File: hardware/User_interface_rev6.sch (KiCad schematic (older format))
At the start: 42 parts, among them IC201 CAT4002ATD-GT3, SW201 F1, SW202 F4, SW203 F7, SW204 ESTOP, SW205 F0, SW206 F2, SW207 F5, SW208 F8, SW209 LOCO1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

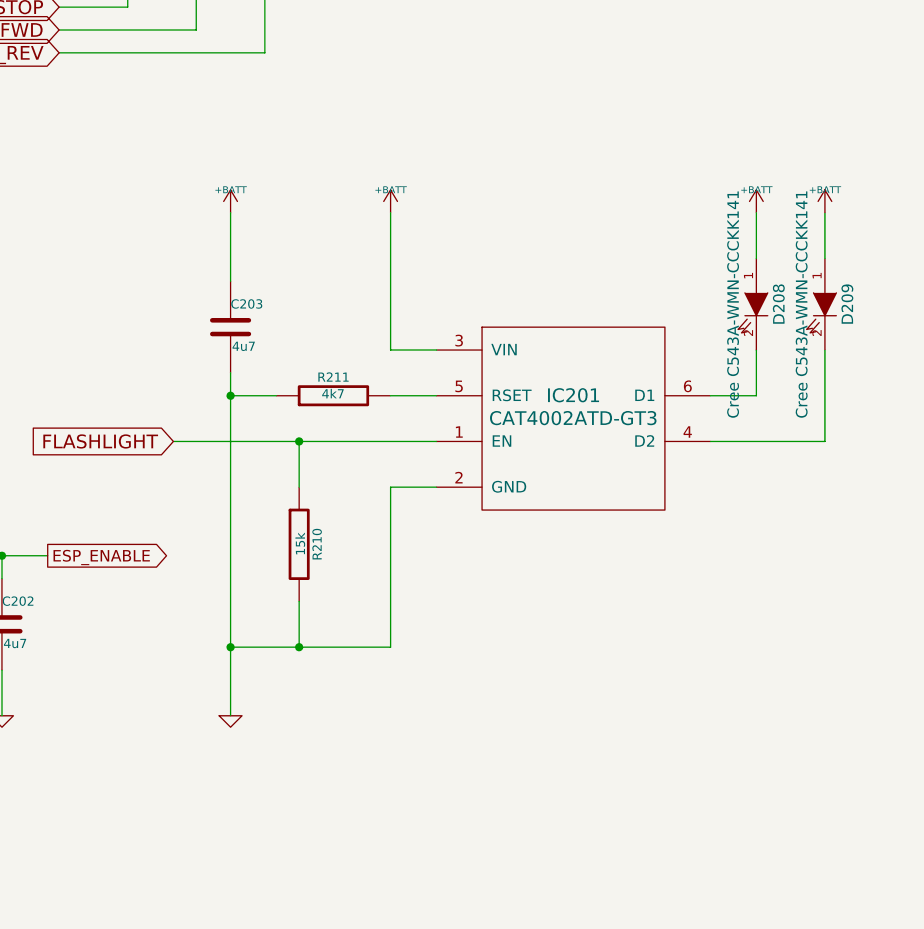
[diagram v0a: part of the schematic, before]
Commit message: Replace CAT4002 with HX4004A...
...for flashlight LEDs.
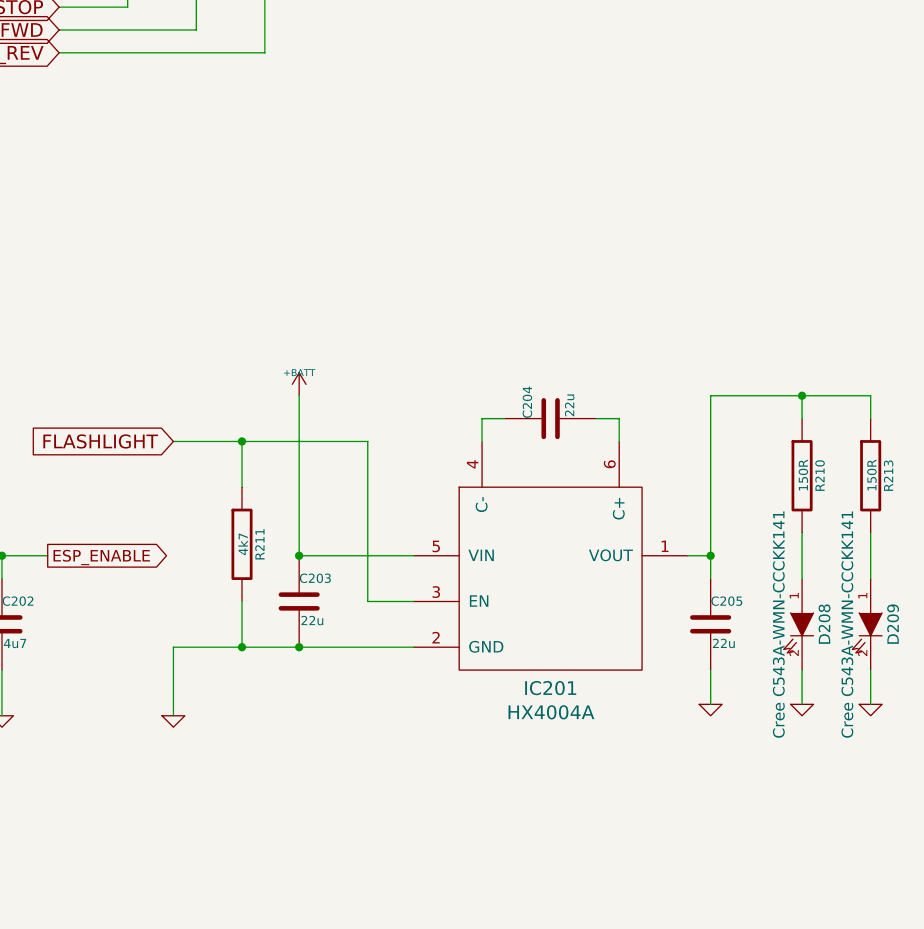
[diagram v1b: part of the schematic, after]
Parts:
- removed IC201: CAT4002ATD-GT3, Package_TO_SOT_SMD:SOT-23-6_Handsoldering, symbol wfred_rev6-rescue:MIC2860-my_devices-wfred_rev2-rescue
- added C204, C205: 22u, Capacitor_SMD:C_0805_2012Metric_Pad1.15x1.40mm_HandSolder, symbol wfred_rev6-rescue:C-RESCUE-wfred_rev2-wfred_rev2-rescue
- added IC201: HX4004A, Package_TO_SOT_SMD:SOT-23-6_Handsoldering, symbol my_devices:HX4002
- added R213: 150R, Resistor_SMD:R_0805_2012Metric_Pad1.15x1.40mm_HandSolder, symbol wfred_rev6-rescue:R-RESCUE-wfred_rev2-wfred_rev2-rescue
- C203: value 4u7 -> 22u; LCSC C1779 -> C45783; Reichelt KEM X5R0805 4,7U -> KEM X5R0805 22U
- R210: value 15k -> 150R; LCSC (none) -> C17471; Reichelt SMD-0805 15,0K -> SMD-0805 150; Remark Do not populate with CAT4002A -> (none)
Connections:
- net +BATT: now also IC201.5 (VIN); no longer D208.1 (A), D209.1 (A)
- net FLASHLIGHT: now also R211.1, IC201.3 (EN); no longer R210.1
- net GND: now also D208.2 (K), D209.2 (K), R211.2, C205.2, IC201.2 (GND); no longer R210.2, R211.1
- new net: D208.1 (A), R210.2
- new net: D209.1 (A), R213.2
- new net: C205.1, IC201.1 (VOUT), R210.1, R213.1
- new net: C204.1, IC201.4 (C-)
- new net: C204.2, IC201.6 (C+)
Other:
- moved on the sheet: D208, D209, R211

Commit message: Change LCSC order number for 22uF caps...
...due to availability.

Also update date and revision number.
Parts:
- C203, C204, C205: LCSC C45783 -> C129303
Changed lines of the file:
@@
 Sheet 2 3
 Title "Wireless FREDI"
-Date "2021-06-28"
-Rev "0.62"
+Date "2022-10-09"
+Rev "0.64"
 Comp "Heiko Rosemann (heiko.rosemann@web.de) CC-BY-SA"
 Comment1 ""
@@
 F 3 "" H 9350 4450 60  0000 C CNN
 F 4 "KEM X5R0805 22U" H 9350 4450 60  0001 C CNN "Reichelt"
-F 5 "C45783" H 9350 4450 50  0001 C CNN "LCSC"
+F 5 "C129303" H 9350 4450 50  0001 C CNN "LCSC"
 	1    9350 4450
 	0    -1   -1   0
@@
 F 3 "" H 10050 5350 60  0000 C CNN
 F 4 "KEM X5R0805 22U" H 10050 5350 60  0001 C CNN "Reichelt"
-F 5 "C45783" H 10050 5350 50  0001 C CNN "LCSC"
+F 5 "C129303" H 10050 5350 50  0001 C CNN "LCSC"
 	1    10050 5350
 	1    0    0    -1
@@
 F 3 "" H 8250 5250 60  0000 C CNN
 F 4 "KEM X5R0805 22U" H 8250 5250 60  0001 C CNN "Reichelt"
-F 5 "C45783" H 8250 5250 50  0001 C CNN "LCSC"
+F 5 "C129303" H 8250 5250 50  0001 C CNN "LCSC"
 	1    8250 5250
 	1    0    0    -1
